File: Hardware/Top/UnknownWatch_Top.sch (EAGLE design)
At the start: 55 parts, among them SW6 SWITCH.MOM, SW7 SWITCH.MOM, SW8 SWITCH.MOM, U2 NRF52832_MODULE_MDBT42, U4 PCF8523, U5 PHOTOTRANSISTOR

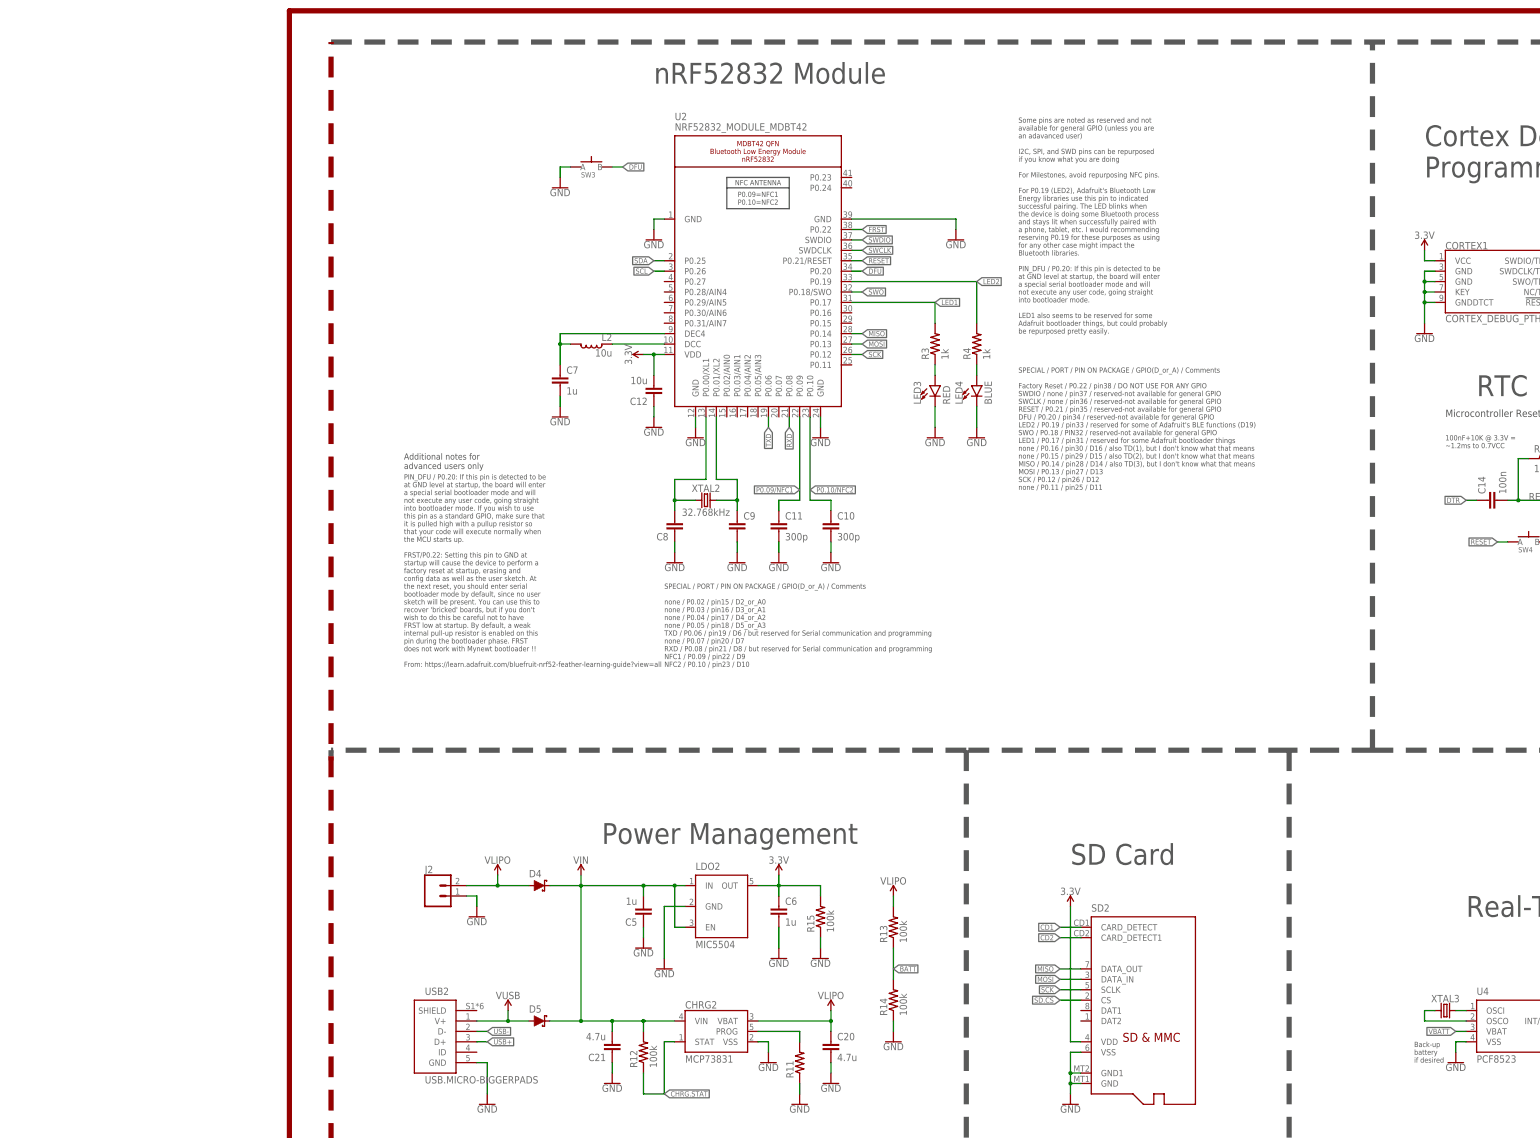
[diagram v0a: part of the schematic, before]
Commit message: Added a comment of all the pins that need to be kept track of.
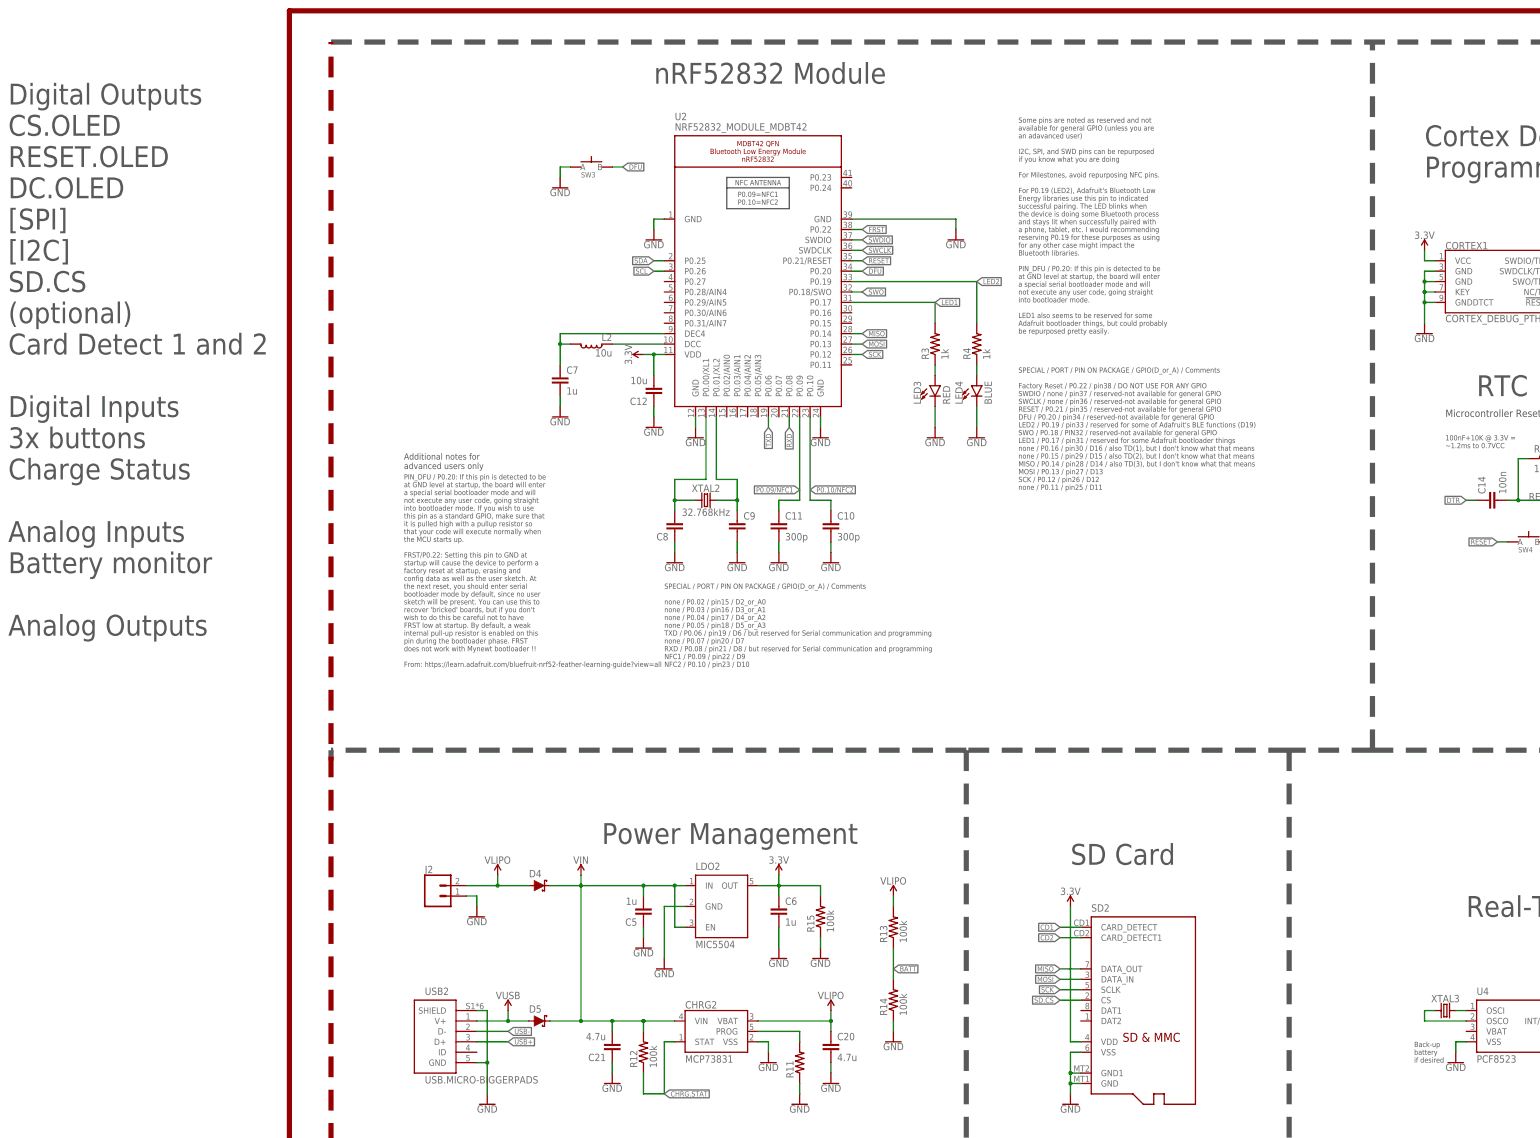
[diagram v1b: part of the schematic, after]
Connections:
- removed net VBATT: U4.VBAT
- net GND: now also USB2.SHIELD
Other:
- note added: "Digital Outputs CS.OLED RESET.OLED DC.OLED [SPI] [I2C] SD.CS (optional) Card Detect 1 and 2 Digital Inputs 3x buttons Charge Status Analog Inputs Battery monitor Analog Outputs"
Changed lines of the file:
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@@
 <wire x1="340.36" y1="5.08" x2="340.36" y2="-96.52" width="1.27" layer="97" style="longdash"/>
 <wire x1="142.24" y1="-99.06" x2="144.78" y2="-99.06" width="1.27" layer="97" style="longdash"/>
-<wire x1="223.52" y1="5.08" x2="213.36" y2="5.08" width="1.27" layer="97" style="longdash"/>
 <wire x1="203.2" y1="5.08" x2="124.46" y2="5.08" width="1.27" layer="97" style="longdash"/>
 <wire x1="124.46" y1="5.08" x2="-30.48" y2="5.08" width="1.27" layer="97" style="longdash"/>
 <wire x1="124.46" y1="5.08" x2="124.46" y2="-99.06" width="1.27" layer="97" style="longdash"/>
 <wire x1="124.46" y1="-99.06" x2="121.92" y2="-99.06" width="1.27" layer="97" style="longdash"/>
-<wire x1="213.36" y1="5.08" x2="203.2" y2="5.08" width="1.27" layer="97" style="longdash"/>
+<wire x1="223.52" y1="5.08" x2="203.2" y2="5.08" width="1.27" layer="97" style="longdash"/>
 <wire x1="203.2" y1="5.08" x2="203.2" y2="-96.52" width="1.27" layer="97" style="longdash"/>
+<text x="-109.22" y="33.02" size="5.08" layer="97">Digital Outputs
+CS.OLED
+RESET.OLED
+DC.OLED
+[SPI]
+[I2C]
+SD.CS
+(optional)
+Card Detect 1 and 2
+Digital Inputs
+3x buttons
+Charge Status
+Analog Inputs
+Battery monitor
+Analog Outputs</text>
 </plain>
 <instances>
@@
 <pinref part="GND40" gate="G$1" pin="GND"/>
 <wire x1="7.62" y1="-71.12" x2="7.62" y2="-78.74" width="0.1524" layer="91"/>
+<pinref part="USB2" gate="G$1" pin="SHIELD"/>
+<wire x1="5.08" y1="-58.42" x2="7.62" y2="-58.42" width="0.1524" layer="91"/>
+<wire x1="7.62" y1="-58.42" x2="7.62" y2="-71.12" width="0.1524" layer="91"/>
+<junction x="7.62" y="-71.12"/>
 </segment>
 <segment>
@@
 <segment>
 <pinref part="USB2" gate="G$1" pin="D-"/>
-<wire x1="5.08" y1="-63.5" x2="7.62" y2="-63.5" width="0.1524" layer="91"/>
-<label x="7.62" y="-63.5" size="1.27" layer="95" xref="yes"/>
+<wire x1="5.08" y1="-63.5" x2="12.7" y2="-63.5" width="0.1524" layer="91"/>
+<label x="12.7" y="-63.5" size="1.27" layer="95" xref="yes"/>
 </segment>
 </net>
@@
 <segment>
 <pinref part="USB2" gate="G$1" pin="D+"/>
-<wire x1="5.08" y1="-66.04" x2="7.62" y2="-66.04" width="0.1524" layer="91"/>
-<label x="7.62" y="-66.04" size="1.27" layer="95" xref="yes"/>
+<wire x1="5.08" y1="-66.04" x2="12.7" y2="-66.04" width="0.1524" layer="91"/>
+<label x="12.7" y="-66.04" size="1.27" layer="95" xref="yes"/>
 </segment>
 </net>
@@
 </segment>
 </net>
-<net name="VBATT" class="0">
-<segment>
-<wire x1="246.38" y1="-63.5" x2="243.84" y2="-63.5" width="0.1524" layer="91"/>
-<label x="243.84" y="-63.5" size="1.27" layer="95" rot="R180" xref="yes"/>
-<pinref part="U4" gate="G$1" pin="VBAT"/>
-</segment>
-</net>

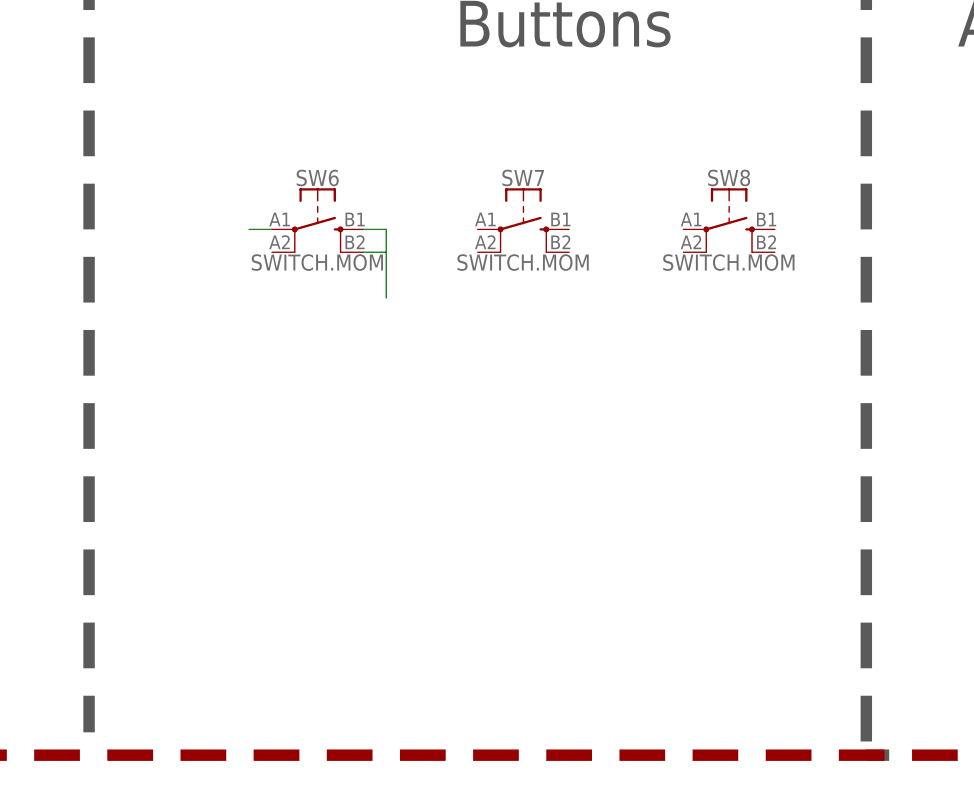
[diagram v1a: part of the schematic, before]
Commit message: Made changes to buttons
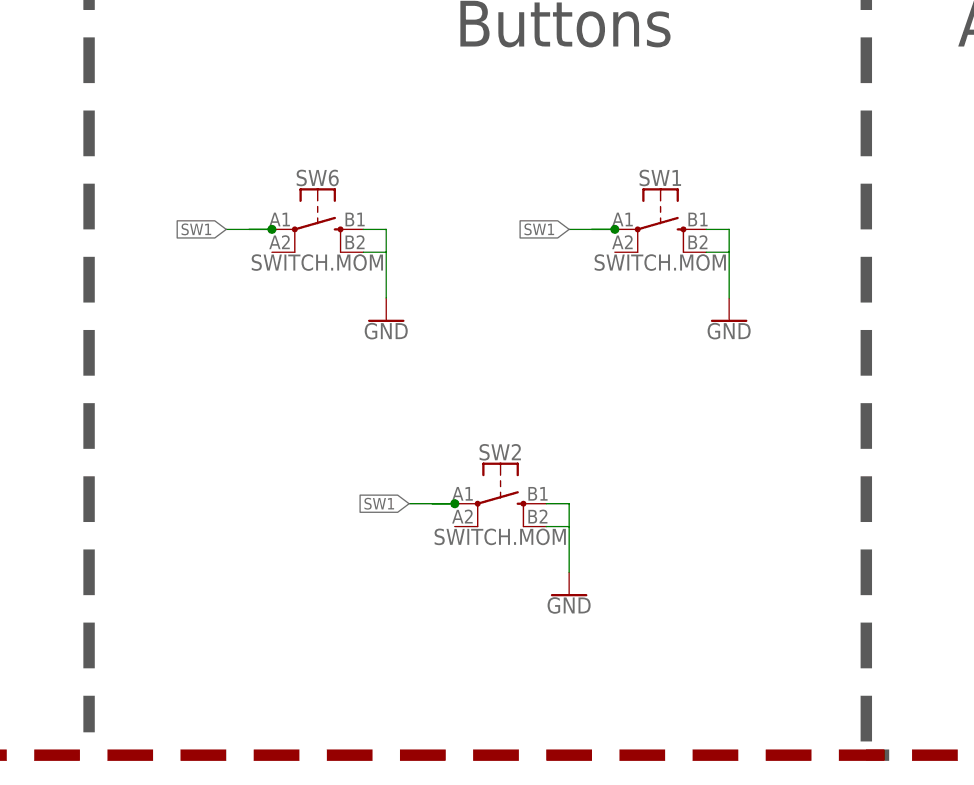
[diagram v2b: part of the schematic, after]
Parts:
- removed SW7, SW8: SWITCH.MOM, LinnesLab-Switches:SWITCH.MOM
- added SW1, SW2: SWITCH.MOM, LinnesLab-Switches:SWITCH.MOM
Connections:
- removed net N$16: SW6.3, SW6.4
- removed net N$18: SW6.1
- new net SW1: SW1.1, SW2.1, SW6.1
- net GND: now also SW1.3, SW1.4, SW2.3, SW2.4, SW6.3, SW6.4
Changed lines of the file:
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@@
 <part name="SUPPLY7" library="LinnesLab-Symbols" deviceset="3.3V" device=""/>
 <part name="SW6" library="LinnesLab-Switches" deviceset="SWITCH.MOM" device=""/>
-<part name="SW7" library="LinnesLab-Switches" deviceset="SWITCH.MOM" device=""/>
-<part name="SW8" library="LinnesLab-Switches" deviceset="SWITCH.MOM" device=""/>
+<part name="GND1" library="LinnesLab-Symbols" deviceset="GND" device=""/>
+<part name="SW1" library="LinnesLab-Switches" deviceset="SWITCH.MOM" device=""/>
+<part name="GND6" library="LinnesLab-Symbols" deviceset="GND" device=""/>
+<part name="SW2" library="LinnesLab-Switches" deviceset="SWITCH.MOM" device=""/>
+<part name="GND13" library="LinnesLab-Symbols" deviceset="GND" device=""/>
 </parts>
 <sheets>
@@
 <attribute name="VALUE" x="365.76" y="-43.434" size="1.778" layer="96" font="vector" align="top-center"/>
 </instance>
-<instance part="SW7" gate="G$1" x="388.62" y="-40.64" smashed="yes">
-<attribute name="NAME" x="388.62" y="-35.814" size="1.778" layer="95" font="vector" align="bottom-center"/>
-<attribute name="VALUE" x="388.62" y="-43.434" size="1.778" layer="96" font="vector" align="top-center"/>
-</instance>
-<instance part="SW8" gate="G$1" x="411.48" y="-40.64" smashed="yes">
-<attribute name="NAME" x="411.48" y="-35.814" size="1.778" layer="95" font="vector" align="bottom-center"/>
-<attribute name="VALUE" x="411.48" y="-43.434" size="1.778" layer="96" font="vector" align="top-center"/>
+<instance part="GND1" gate="G$1" x="373.38" y="-50.8" smashed="yes">
+<attribute name="VALUE" x="373.38" y="-51.054" size="1.778" layer="96" align="top-center"/>
+</instance>
+<instance part="SW1" gate="G$1" x="403.86" y="-40.64" smashed="yes">
+<attribute name="NAME" x="403.86" y="-35.814" size="1.778" layer="95" font="vector" align="bottom-center"/>
+<attribute name="VALUE" x="403.86" y="-43.434" size="1.778" layer="96" font="vector" align="top-center"/>
+</instance>
+<instance part="GND6" gate="G$1" x="411.48" y="-50.8" smashed="yes">
+<attribute name="VALUE" x="411.48" y="-51.054" size="1.778" layer="96" align="top-center"/>
+</instance>
+<instance part="SW2" gate="G$1" x="386.08" y="-71.12" smashed="yes">
+<attribute name="NAME" x="386.08" y="-66.294" size="1.778" layer="95" font="vector" align="bottom-center"/>
+<attribute name="VALUE" x="386.08" y="-73.914" size="1.778" layer="96" font="vector" align="top-center"/>
+</instance>
+<instance part="GND13" gate="G$1" x="393.7" y="-81.28" smashed="yes">
+<attribute name="VALUE" x="393.7" y="-81.534" size="1.778" layer="96" align="top-center"/>
 </instance>
 </instances>
@@
 <wire x1="459.74" y1="-63.5" x2="459.74" y2="-60.96" width="0.1524" layer="91"/>
 <junction x="459.74" y="-60.96"/>
+</segment>
+<segment>
+<pinref part="SW6" gate="G$1" pin="3"/>
+<wire x1="370.84" y1="-40.64" x2="373.38" y2="-40.64" width="0.1524" layer="91"/>
+<wire x1="373.38" y1="-40.64" x2="373.38" y2="-43.18" width="0.1524" layer="91"/>
+<pinref part="SW6" gate="G$1" pin="4"/>
+<wire x1="373.38" y1="-48.26" x2="373.38" y2="-43.18" width="0.1524" layer="91"/>
+<wire x1="373.38" y1="-43.18" x2="370.84" y2="-43.18" width="0.1524" layer="91"/>
+<pinref part="GND1" gate="G$1" pin="GND"/>
+</segment>
+<segment>
+<pinref part="SW1" gate="G$1" pin="3"/>
+<wire x1="408.94" y1="-40.64" x2="411.48" y2="-40.64" width="0.1524" layer="91"/>
+<wire x1="411.48" y1="-40.64" x2="411.48" y2="-43.18" width="0.1524" layer="91"/>
+<pinref part="SW1" gate="G$1" pin="4"/>
+<wire x1="411.48" y1="-48.26" x2="411.48" y2="-43.18" width="0.1524" layer="91"/>
+<wire x1="411.48" y1="-43.18" x2="408.94" y2="-43.18" width="0.1524" layer="91"/>
+<pinref part="GND6" gate="G$1" pin="GND"/>
+</segment>
+<segment>
+<pinref part="SW2" gate="G$1" pin="3"/>
+<wire x1="391.16" y1="-71.12" x2="393.7" y2="-71.12" width="0.1524" layer="91"/>
+<wire x1="393.7" y1="-71.12" x2="393.7" y2="-73.66" width="0.1524" layer="91"/>
+<pinref part="SW2" gate="G$1" pin="4"/>
+<wire x1="393.7" y1="-78.74" x2="393.7" y2="-73.66" width="0.1524" layer="91"/>
+<wire x1="393.7" y1="-73.66" x2="391.16" y2="-73.66" width="0.1524" layer="91"/>
+<pinref part="GND13" gate="G$1" pin="GND"/>
 </segment>
 </net>
@@
 </segment>
 </net>
-<net name="N$16" class="0">
-<segment>
-<pinref part="SW6" gate="G$1" pin="3"/>
-<wire x1="370.84" y1="-40.64" x2="373.38" y2="-40.64" width="0.1524" layer="91"/>
-<wire x1="373.38" y1="-40.64" x2="373.38" y2="-43.18" width="0.1524" layer="91"/>
-<pinref part="SW6" gate="G$1" pin="4"/>
-<wire x1="373.38" y1="-48.26" x2="373.38" y2="-43.18" width="0.1524" layer="91"/>
-<wire x1="373.38" y1="-43.18" x2="370.84" y2="-43.18" width="0.1524" layer="91"/>
-</segment>
-</net>
-<net name="N$18" class="0">
+<net name="SW1" class="0">
 <segment>
 <pinref part="SW6" gate="G$1" pin="1"/>
 <wire x1="360.68" y1="-40.64" x2="358.14" y2="-40.64" width="0.1524" layer="91"/>
-</segment>
-</net>
+<label x="355.6" y="-40.64" size="1.27" layer="95" rot="R180" xref="yes"/>
+<wire x1="355.6" y1="-40.64" x2="360.68" y2="-40.64" width="0.1524" layer="91"/>
+<junction x="360.68" y="-40.64"/>
+</segment>
+<segment>
+<pinref part="SW1" gate="G$1" pin="1"/>
+<wire x1="398.78" y1="-40.64" x2="396.24" y2="-40.64" width="0.1524" layer="91"/>
+<label x="393.7" y="-40.64" size="1.27" layer="95" rot="R180" xref="yes"/>
+<wire x1="393.7" y1="-40.64" x2="398.78" y2="-40.64" width="0.1524" layer="91"/>
+<junction x="398.78" y="-40.64"/>
+</segment>
+<segment>
+<pinref part="SW2" gate="G$1" pin="1"/>
+<wire x1="381" y1="-71.12" x2="378.46" y2="-71.12" width="0.1524" layer="91"/>
+<label x="375.92" y="-71.12" size="1.27" layer="95" rot="R180" xref="yes"/>
+<wire x1="375.92" y1="-71.12" x2="381" y2="-71.12" width="0.1524" layer="91"/>
+<junction x="381" y="-71.12"/>
+</segment>
+</net>
